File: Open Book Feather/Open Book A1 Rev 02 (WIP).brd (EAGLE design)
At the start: 77.5 x 112.3 mm, 124 parts, among them J1 SJ-43514-SMT, J2 10118193-0001LF, Q1 DMG341, Q2 IRLML0100, SW1 SPDT_SWITCH, U1 AP2112-3.3, U2 MCP73831T-2ACI/OT, U3 ATSAMD51J64-TQFP(10X10), U4 GD25Q16C (or GD25Q32C), U5 74AC165D, U6 GD25Q16C (or GD25Q32C), U7 23K256-I/SN, U8 MAX4466EXK+T, X1 JSTPH, X2 2x5 0.05" SWD

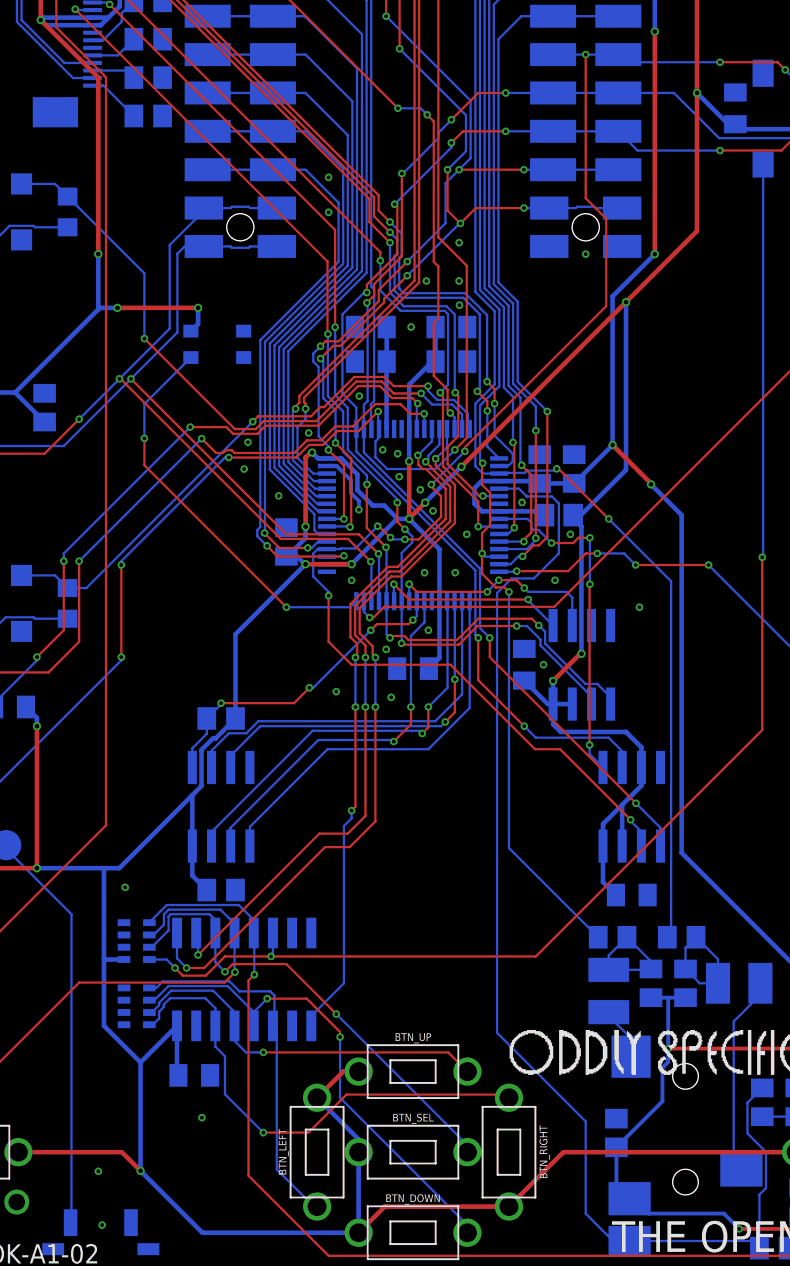
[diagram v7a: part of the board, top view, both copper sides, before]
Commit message: scoot filter caps away from chip (easier for manual rework if needed)
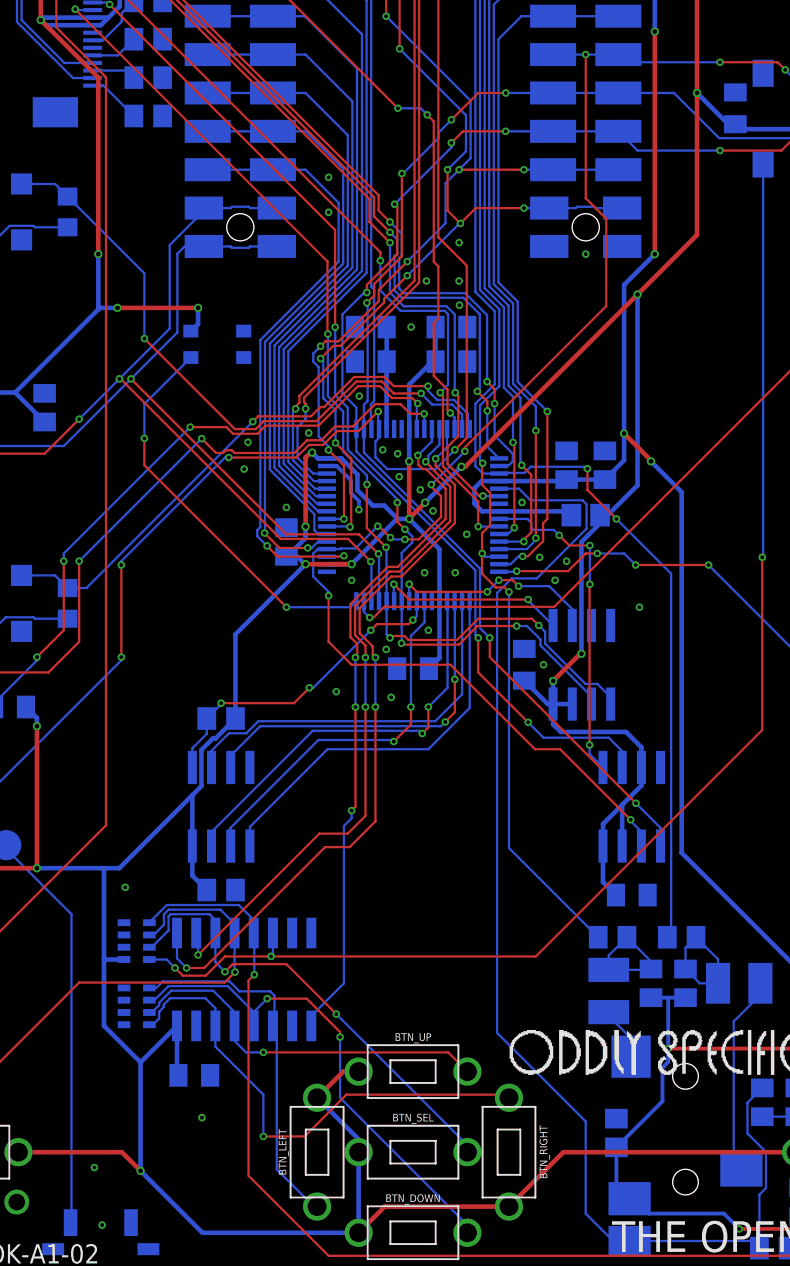
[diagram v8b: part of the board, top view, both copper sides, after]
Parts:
- moved C11 2.05 mm to (51.6, 53.3)
- moved C12 1.80 mm to (49.0, 53.3)
- moved FB1 1.78 mm to (50.3, 50.0)
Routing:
- net AVCC: track 129.8 -> 132.9 mm
- net A7_MIC: track 80.5 -> 83.2 mm
- net A0: track 91.4 -> 92.6 mm
- net UNIFONT_CS: track 22.6 -> 22.0 mm
- net +3V3: track 531.2 -> 531.7 mm
- net GND: vias 49 -> 50
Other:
- board text added: "Bits: 0: LEFT 1: DOWN 2: UP 3: RIGHT 4: SEL 5: PREV 6: NEXT 7: SD"
- board text added: "R26-R27: pull-up & pull-down resistor arrays."
- board text added: "card detect"
- board text removed: "Bits: 0: LEFT 1: DOWN 2: UP 3: RIGHT 4: SEL 5: PREV 6: NEXT 7: SD Card Detect"
